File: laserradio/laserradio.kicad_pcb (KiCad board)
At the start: 2 copper layers, 68.6 x 43.7 mm, 89 parts, among them J1 USB4105-GF-A, J3 DEBUG, J4 RIGHT, SW1 SW_SPDT, SW2 SW_SPDT, U1 W25Q128JV, U2 RP2040, U3 MCP1702T-3302E_CB, U4 ADA4891, U5 RS2255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

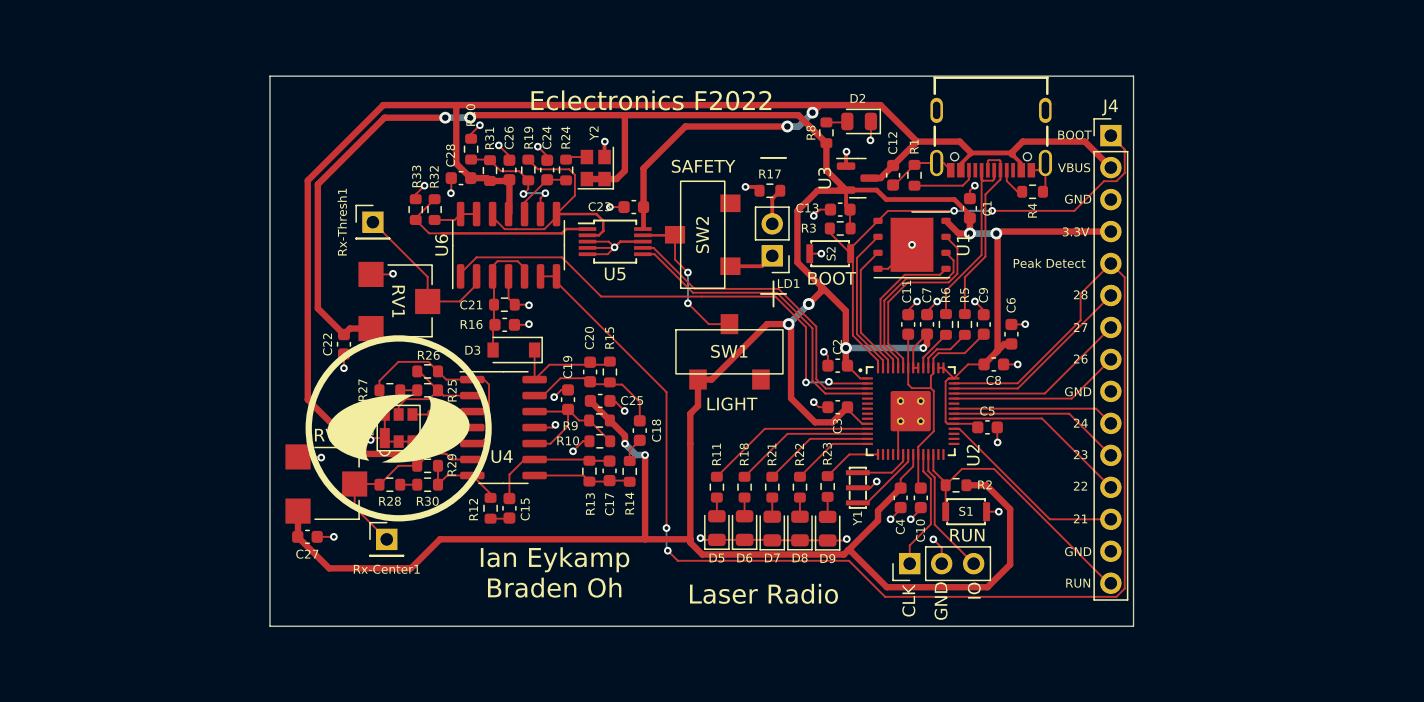
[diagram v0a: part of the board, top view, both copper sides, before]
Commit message: add mounting holes
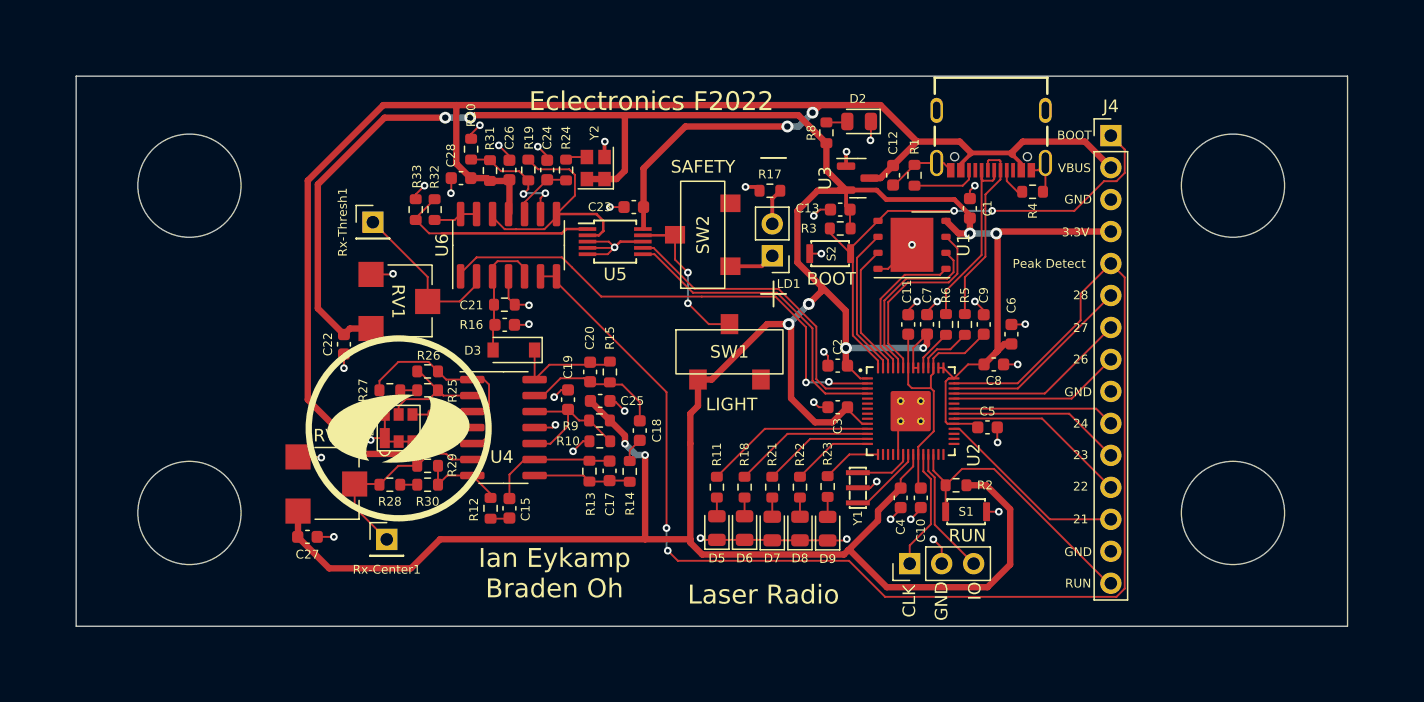
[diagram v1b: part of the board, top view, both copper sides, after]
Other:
- board size 68.6 x 43.7 mm -> 101 x 43.7 mm
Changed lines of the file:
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@@
   (gr_line (start 102.4 90.6) (end 104.4 90.6) (layer "F.SilkS") (width 0.15))
   (gr_line (start 102.4 79.8) (end 104.4 79.8) (layer "F.SilkS") (width 0.15))
-  (gr_rect (start 132 73.3) (end 63.4 117) (layer "Edge.Cuts") (width 0.1) (fill none))
+  (gr_circle (center 139.9 108) (end 144 108) (layer "Edge.Cuts") (width 0.1) (fill none))
+  (gr_rect (start 149 73.3) (end 48 117) (layer "Edge.Cuts") (width 0.1) (fill none))
+  (gr_circle (center 57 108) (end 61.1 108) (layer "Edge.Cuts") (width 0.1) (fill none))
+  (gr_circle (center 57 82) (end 61.1 82) (layer "Edge.Cuts") (width 0.1) (fill none))
+  (gr_circle (center 139.9 82) (end 144 82) (layer "Edge.Cuts") (width 0.1) (fill none))
   (gr_text "Never Gonna \nGive You Up" (at 114.4524 114.046) (layer "B.SilkS")
     (effects (font (size 1 1) (thickness 0.15)) (justify mirror))

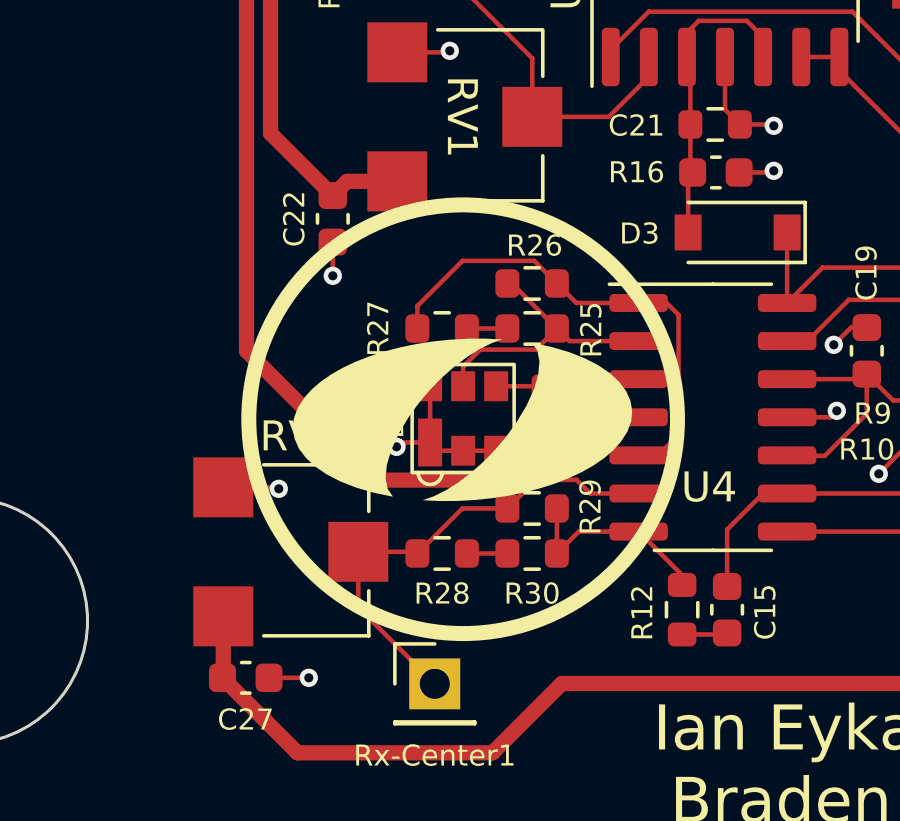
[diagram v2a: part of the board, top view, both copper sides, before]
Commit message: switch footprint for photodiode
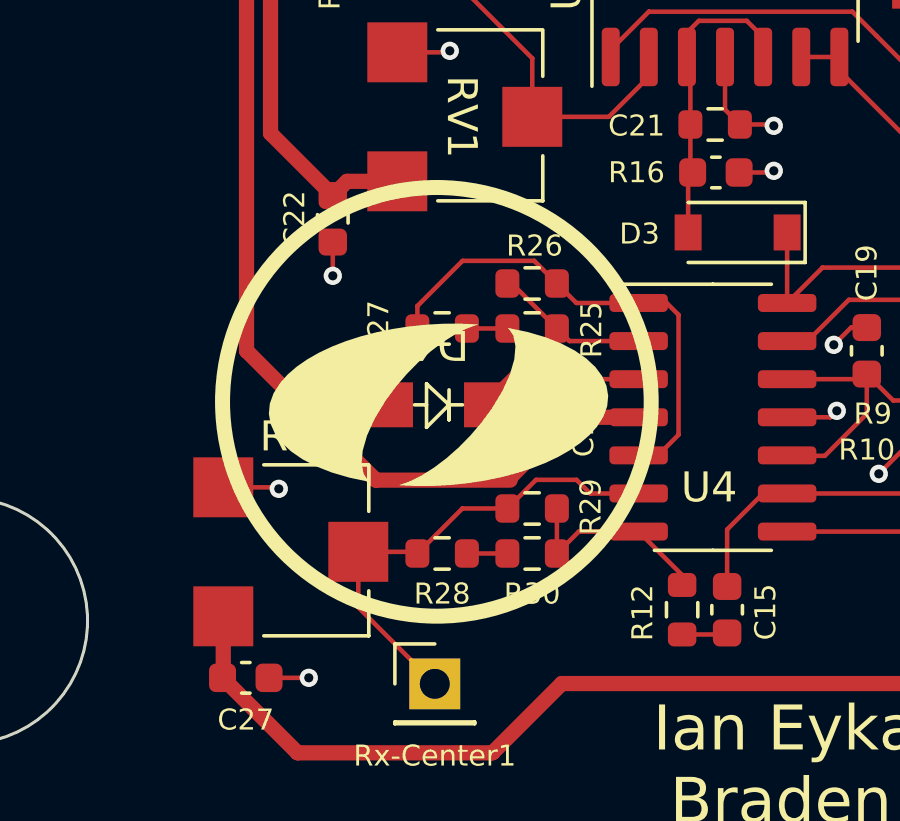
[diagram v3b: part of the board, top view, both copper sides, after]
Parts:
- D4: footprint Eclectronics:Photodiode -> Eclectronics:Laser_photodiode_2_pad
- R10: value 330k -> 316k
- R13, R17: value 1k -> 1K
- R19, R32: value 5k -> 4.99k
- R24: value 1.2k -> 1.1k
- R5, R6: value 27Ω -> 30
- moved OlinLogoLg 0.94 mm to (72.8, 100.8)
- moved D4 0.94 mm to (72.8, 100.8), turned to 180 degrees
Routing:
- net GND: track 99.6 -> 94.1 mm
- net Net-(D4-Pad1): track 9.47 -> 8.69 mm
